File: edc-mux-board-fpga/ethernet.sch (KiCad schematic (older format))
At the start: 1 part, among them U55 W5500

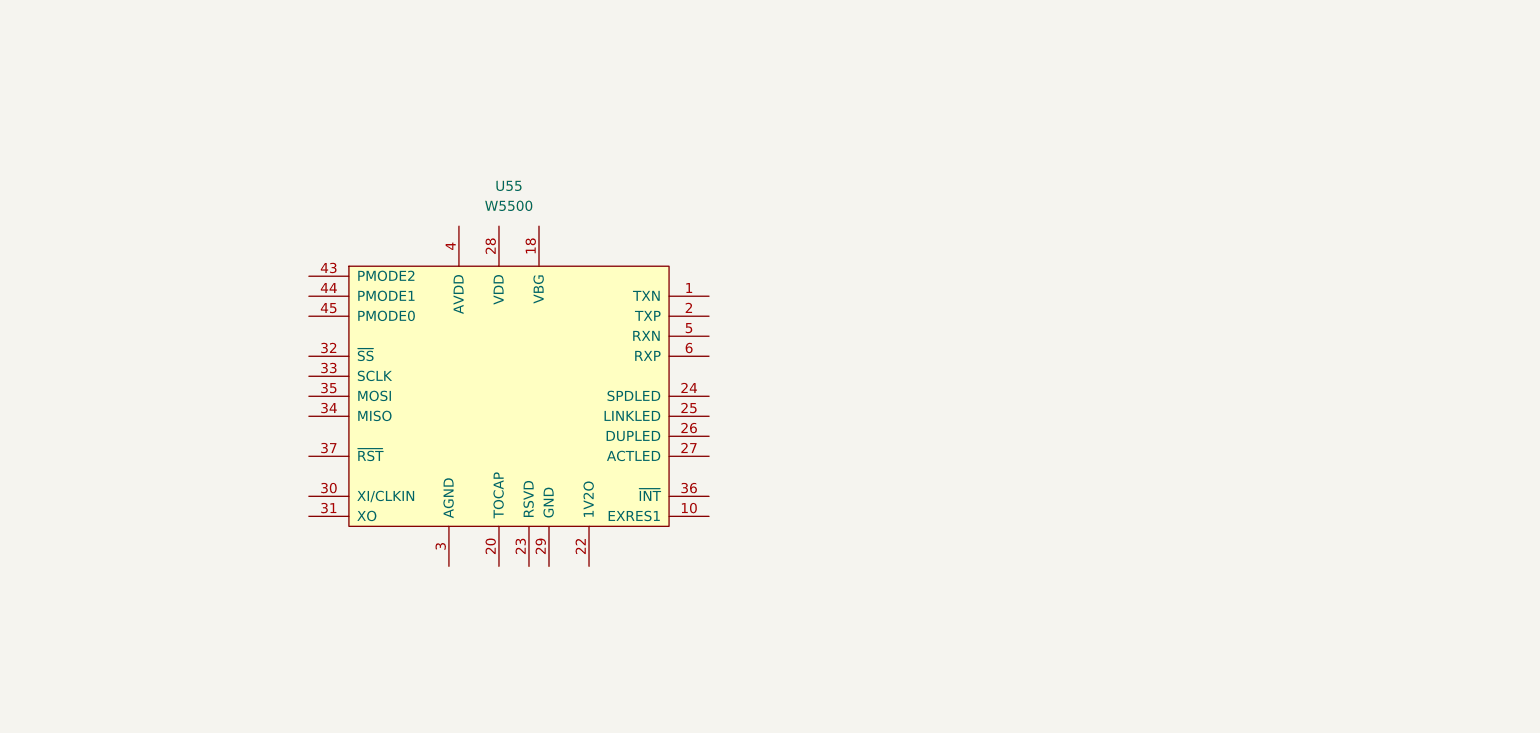
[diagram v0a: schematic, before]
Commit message: mostly finished ethernet schematic
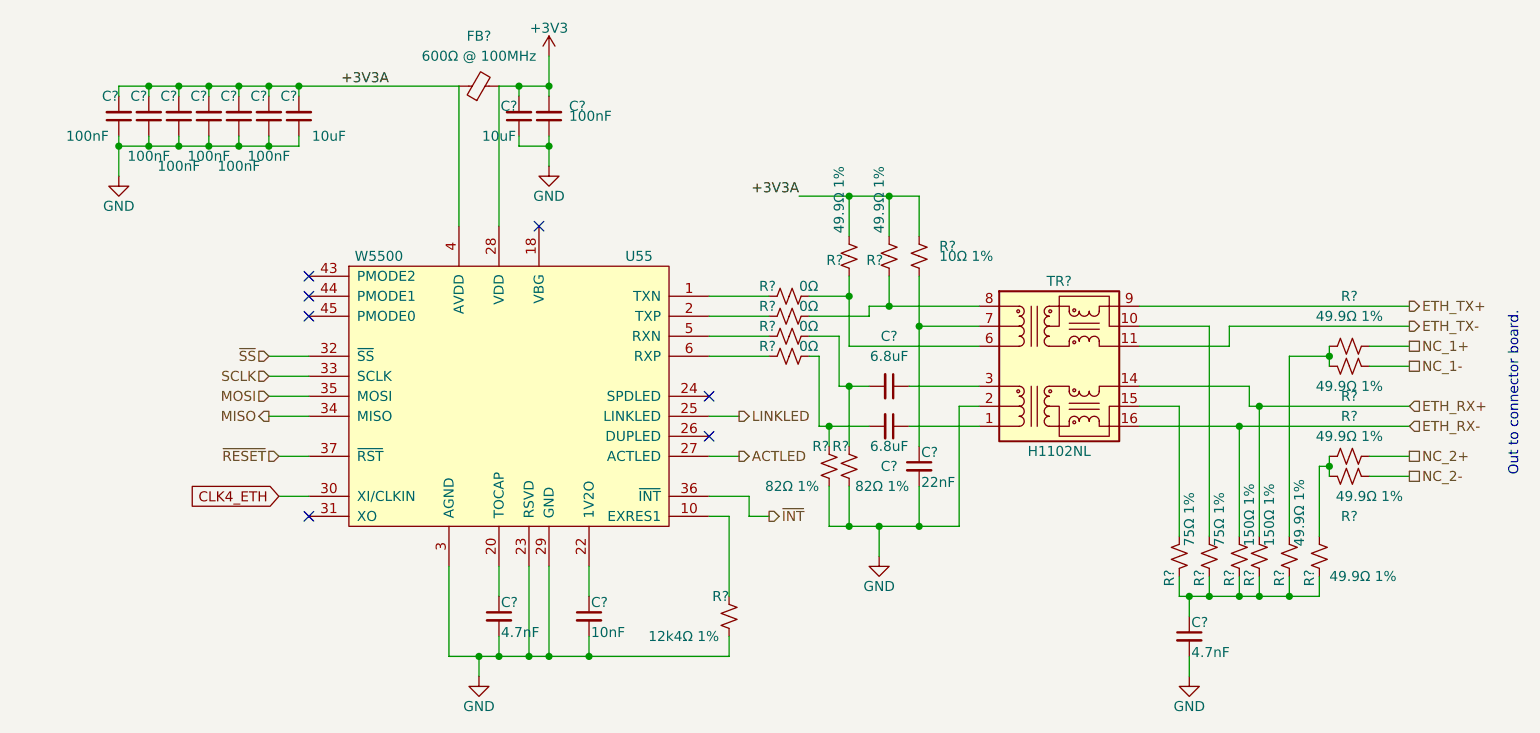
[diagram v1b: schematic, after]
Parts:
- added C?: 22nF, symbol Device:C_Small
- added C? (x2): 6.8uF, symbol Device:C_Small
- added C? (x2): 4.7nF, symbol Device:C_Small
- added C?: 10nF, symbol Device:C_Small
- added C? (x7): 100nF, symbol Device:C_Small
- added C? (x2): 10uF, symbol Device:C_Small
- added FB?: 600Ω @ 100MHz, Capacitor_SMD:C_0805_2012Metric, symbol Device:Ferrite_Bead_Small
- added R? (x4): 0Ω, symbol Device:R_Small_US
- added R? (x8): 49.9Ω 1%, symbol Device:R_Small_US
- added R?: 10Ω 1%, symbol Device:R_Small_US
- added R? (x2): 82Ω 1%, symbol Device:R_Small_US
- added R? (x2): 75Ω 1%, symbol Device:R_Small_US
- added R? (x2): 150Ω 1%, symbol Device:R_Small_US
- added R?: 12k4Ω 1%, symbol Device:R_Small_US
- added TR?: H1102NL, Transformer_SMD:Transformer_Pulse_H1100NL, symbol Transformer:PT61017PEL
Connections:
- net at U55.1 (TXN): now also R?.2
- net at U55.10 (EXRES1): now also R?.2
- net +3V3A: now reaches U55.11 (AVDD), U55.15 (AVDD), U55.17 (AVDD), U55.21 (AVDD), U55.4 (AVDD), U55.8 (AVDD)
- net +3V3A: now also C?.2, C?.2, C?.2, C?.2, C?.2, C?.2, C?.2, FB?.1, R?.2, R?.2, R?.2
- net GND: now reaches U55.14 (AGND), U55.16 (AGND), U55.19 (AGND), U55.3 (AGND), U55.48 (AGND), U55.9 (AGND)
- net GND: now also U55.23 (RSVD), U55.29 (GND), C?.1, C?.1, C?.1, C?.1, C?.1, C?.1, C?.1, C?.1, C?.1, C?.2, C?.2, C?.2, C?.2, R?.1, R?.1, R?.1, TR?.2 (C_TD)
- net at U55.2 (TXP): now also R?.2
- net at U55.20 (TOCAP): now also C?.1
- net at U55.22 (1V2O): now also C?.1
- net LINKLED: now reaches U55.25 (LINKLED)
- net ACTLED: now reaches U55.27 (ACTLED)
- net +3V3: now reaches U55.28 (VDD)
- net +3V3: now also C?.2, C?.2, FB?.2
- net CLK4_ETH: now reaches U55.30 (XI/CLKIN)
- net ~SS: now reaches U55.32 (~SS)
- net SCLK: now reaches U55.33 (SCLK)
- net MISO: now reaches U55.34 (MISO)
- net MOSI: now reaches U55.35 (MOSI)
- net ~INT: now reaches U55.36 (~INT)
- net ~RESET: now reaches U55.37 (~RST)
- net at U55.5 (RXN): now also R?.2
- net at U55.6 (RXP): now also R?.2
- new net: C?.1, TR?.1 (TD+)
- new net: R?.2, TR?.10 (C_RX)
- new net: R?.2, TR?.15 (C_TX)
- new net: C?.1, TR?.3 (TD-)
- new net: R?.1, R?.1, TR?.6 (RD+)
- new net: C?.1, R?.1, TR?.7 (C_RD)
- new net: R?.1, R?.1, TR?.8 (RD-)
- new net: C?.2, R?.1, R?.2 (x2)
- new net: C?.1, R?.1, R?.1, R?.1, R?.1, R?.1, R?.1
- new net: R?.1, R?.1, R?.2 (x2)
- new net ETH_RX+: R?.2, TR?.14 (TX-)
- new net ETH_RX-: R?.2, TR?.16 (TX+)
- new net ETH_TX+: TR?.9 (RX-)
- new net ETH_TX-: TR?.11 (RX+)
- new net NC_1+: R?.2
- new net NC_1-: R?.2
- new net NC_2+: R?.2
- new net NC_2-: R?.2
- no-connect marks 0 -> 7
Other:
- note added: "Out to connector board."

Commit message: unannotated components after major changes
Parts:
- renumbered U55 to U?
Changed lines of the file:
@@
 P 6000 3250
 AR Path="/5CAA05B1" Ref="U?"  Part="1"
-AR Path="/5CA9FC45/5CAA05B1" Ref="U55"  Part="1"
-F 0 "U55" H 6650 3950 50  0000 C CNN
+AR Path="/5CA9FC45/5CAA05B1" Ref="U?"  Part="1"
+F 0 "U?" H 6650 3950 50  0000 C CNN
 F 1 "W5500" H 5350 3950 50  0000 C CNN
 F 2 "Package_QFP:TQFP-48_7x7mm_P0.5mm" H 7700 5200 50  0001 C CNN

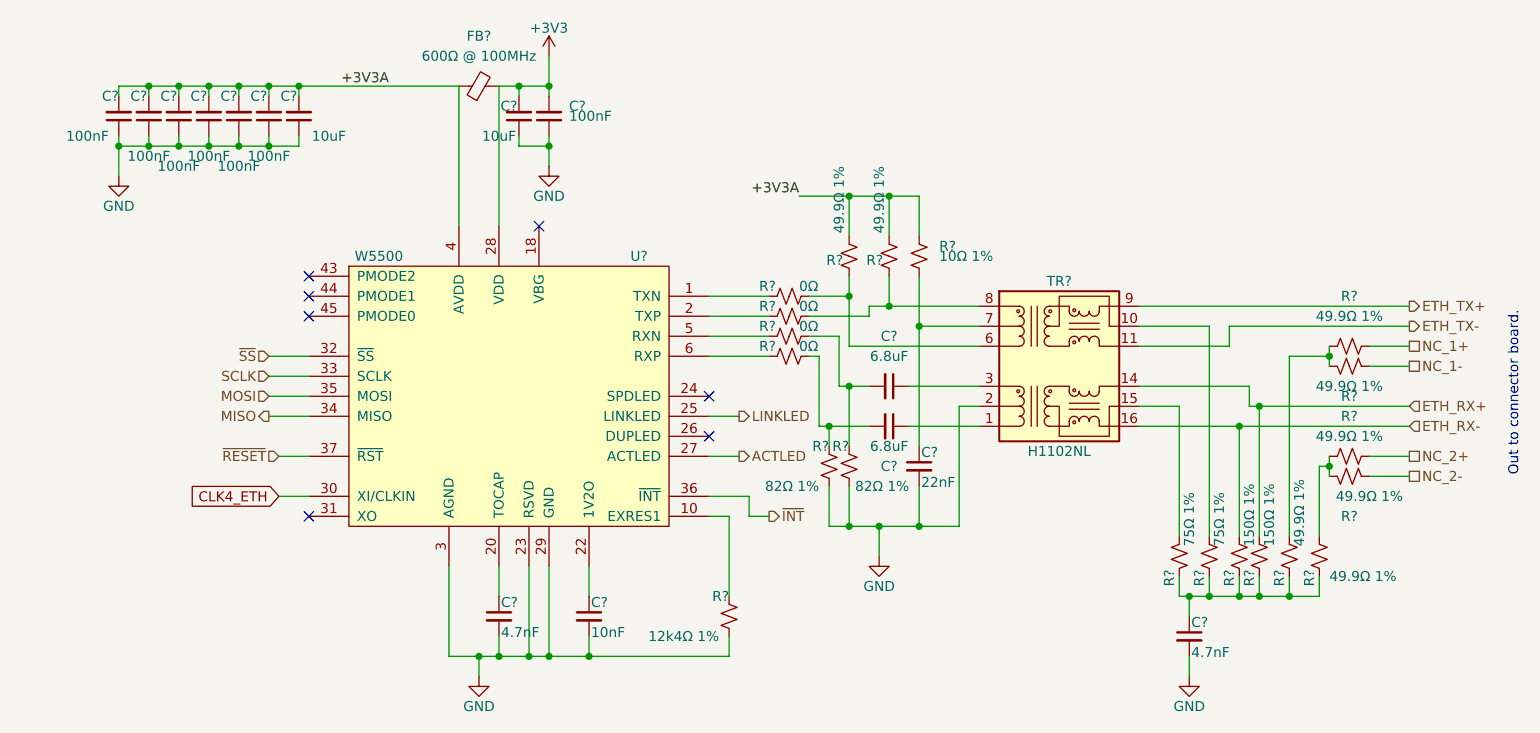
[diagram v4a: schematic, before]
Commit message: Finished FPGA and MCU interconnections.
Finished up interrupt wiring
Fixed a few missing connections
Annotated Schematic
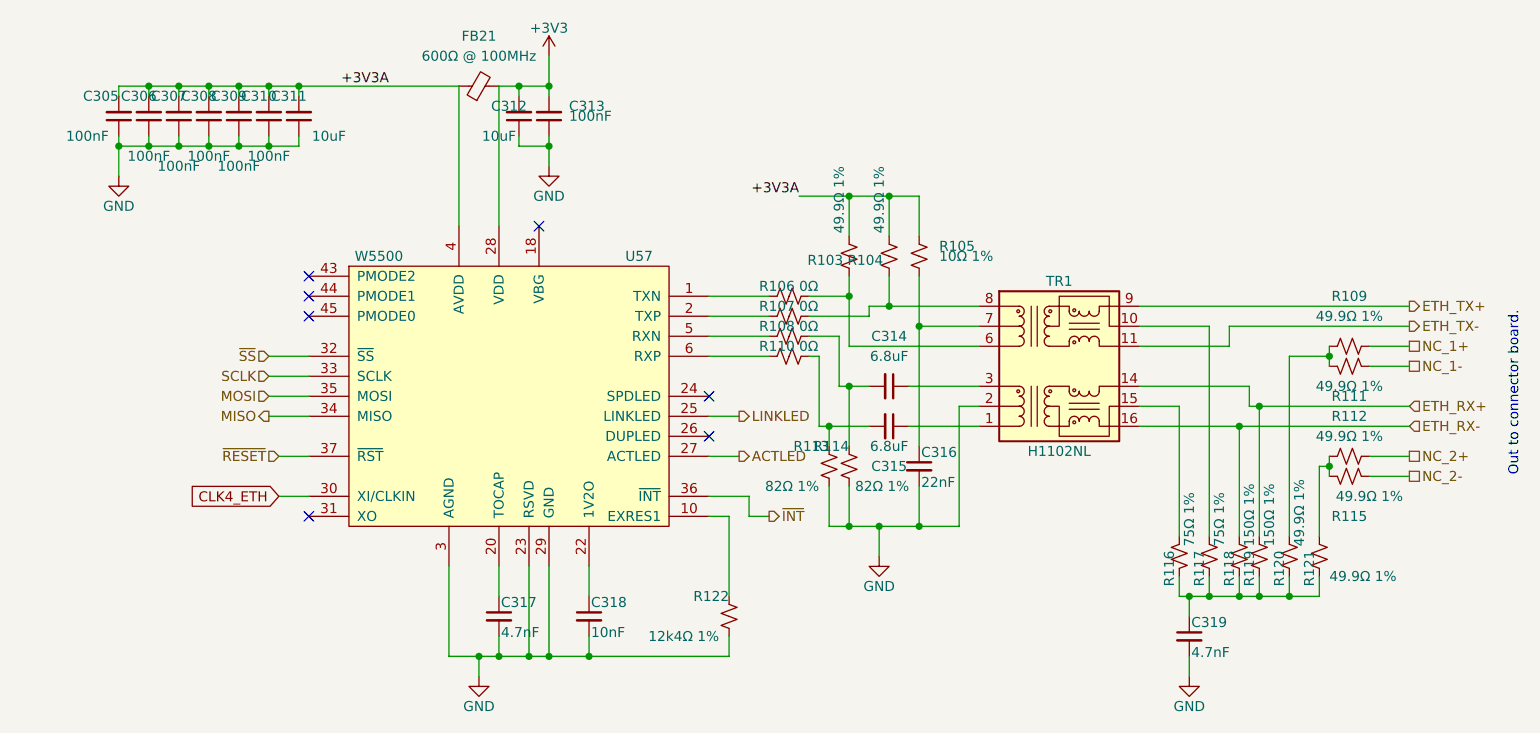
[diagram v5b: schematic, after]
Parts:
- gave numbers to parts that had none: 38
